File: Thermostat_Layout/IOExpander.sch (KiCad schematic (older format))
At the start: 9 parts, among them J5 Conn_01x04, J6 Conn_01x10, U10 TLP3545, U4 MCP23S17_SO, U8 TLP3545, U9 TLP3545

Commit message: Update schematic
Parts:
- renumbered J5 to J3, J6 to J4, R12 to R10, R10 to R8, R11 to R9, U8 to U5, U4 to U6, U9 to U7, U10 to U8
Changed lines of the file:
@@
 $EndDescr
 $Comp
-L Interface_Expansion:MCP23S17_SO U4
+L Interface_Expansion:MCP23S17_SO U6
 U 1 1 5D3F3897
 P 3750 2800
-F 0 "U4" H 3750 4081 50  0000 C CNN
+F 0 "U6" H 3750 4081 50  0000 C CNN
 F 1 "MCP23S17_SO" H 3750 3990 50  0000 C CNN
 F 2 "Package_SO:SOIC-28W_7.5x17.9mm_P1.27mm" H 3950 1800 50  0001 L CNN
@@
 Connection ~ 3000 3600
 $Comp
-L SparkFun-PowerSymbols:GND #GND0108
+L SparkFun-PowerSymbols:GND #GND012
 U 1 1 5D3F48BE
 P 3750 3900
-F 0 "#GND0108" H 3800 3850 45  0001 L BNN
+F 0 "#GND012" H 3800 3850 45  0001 L BNN
 F 1 "GND" H 3750 3730 45  0000 C CNN
 F 2 "" H 3750 3800 60  0001 C CNN
@@
 Connection ~ 3750 3900
 $Comp
-L SparkFun-PowerSymbols:3.3V #SUPPLY0105
+L SparkFun-PowerSymbols:3.3V #SUPPLY07
 U 1 1 5D3F4F5E
 P 3750 1700
-F 0 "#SUPPLY0105" H 3800 1700 45  0001 L BNN
+F 0 "#SUPPLY07" H 3800 1700 45  0001 L BNN
 F 1 "3.3V" H 3750 1976 45  0000 C CNN
 F 2 "XXX-00000" H 3750 1881 60  0000 C CNN
@@
 	5000 2300 4450 2300
 $Comp
-L Connector_Generic:Conn_01x10 J6
+L Connector_Generic:Conn_01x10 J4
 U 1 1 5D49FB9C
 P 8900 2250
-F 0 "J6" H 8980 2242 50  0000 L CNN
+F 0 "J4" H 8980 2242 50  0000 L CNN
 F 1 "Conn_01x10" H 8980 2151 50  0000 L CNN
 F 2 "Connector_JST:JST_PH_S10B-PH-SM4-TB_1x10-1MP_P2.00mm_Horizontal" H 8900 2250 50  0001 C CNN
@@
 	8700 2550 8000 2550
 $Comp
-L SparkFun-PowerSymbols:GND #GND0118
+L SparkFun-PowerSymbols:GND #GND014
 U 1 1 5D4A3239
 P 8700 2750
-F 0 "#GND0118" H 8750 2700 45  0001 L BNN
+F 0 "#GND014" H 8750 2700 45  0001 L BNN
 F 1 "GND" H 8700 2580 45  0000 C CNN
 F 2 "" H 8700 2650 60  0001 C CNN
@@
 UNUSED_BTN
 $Comp
-L Relay_SolidState:TLP3545 U8
+L Relay_SolidState:TLP3545 U5
 U 1 1 5D4AAA5A
 P 2900 5650
-F 0 "U8" H 2900 5975 50  0000 C CNN
+F 0 "U5" H 2900 5975 50  0000 C CNN
 F 1 "TLP3545" H 2900 5884 50  0000 C CNN
 F 2 "Package_DIP:DIP-6_W7.62mm" H 2900 5350 50  0001 C CNN
@@
 $EndComp
 $Comp
-L Relay_SolidState:TLP3545 U9
+L Relay_SolidState:TLP3545 U7
 U 1 1 5D4B0D89
 P 4000 5650
-F 0 "U9" H 4000 5975 50  0000 C CNN
+F 0 "U7" H 4000 5975 50  0000 C CNN
 F 1 "TLP3545" H 4000 5884 50  0000 C CNN
 F 2 "Package_DIP:DIP-6_W7.62mm" H 4000 5350 50  0001 C CNN
@@
 $EndComp
 $Comp
-L Relay_SolidState:TLP3545 U10
+L Relay_SolidState:TLP3545 U8
 U 1 1 5D4B27F7
 P 5100 5650
-F 0 "U10" H 5100 5975 50  0000 C CNN
+F 0 "U8" H 5100 5975 50  0000 C CNN
 F 1 "TLP3545" H 5100 5884 50  0000 C CNN
 F 2 "Package_DIP:DIP-6_W7.62mm" H 5100 5350 50  0001 C CNN
@@
 $EndComp
 $Comp
-L Device:R_US R10
+L Device:R_US R8
 U 1 1 5D4B3F71
 P 2450 5900
-F 0 "R10" H 2518 5946 50  0000 L CNN
+F 0 "R8" H 2518 5946 50  0000 L CNN
 F 1 "100Ω" H 2518 5855 50  0000 L CNN
 F 2 "Resistor_SMD:R_0402_1005Metric" V 2490 5890 50  0001 C CNN
@@
 $EndComp
 $Comp
-L Device:R_US R11
+L Device:R_US R9
 U 1 1 5D4B4905
 P 3550 5900
-F 0 "R11" H 3618 5946 50  0000 L CNN
+F 0 "R9" H 3618 5946 50  0000 L CNN
 F 1 "100Ω" H 3618 5855 50  0000 L CNN
 F 2 "Resistor_SMD:R_0402_1005Metric" V 3590 5890 50  0001 C CNN
@@
 $EndComp
 $Comp
-L Device:R_US R12
+L Device:R_US R10
 U 1 1 5D4B5111
 P 4650 5900
-F 0 "R12" H 4718 5946 50  0000 L CNN
+F 0 "R10" H 4718 5946 50  0000 L CNN
 F 1 "100Ω" H 4718 5855 50  0000 L CNN
 F 2 "Resistor_SMD:R_0402_1005Metric" V 4690 5890 50  0001 C CNN
@@
 	4650 5750 4800 5750
 $Comp
-L SparkFun-PowerSymbols:GND #GND0119
+L SparkFun-PowerSymbols:GND #GND010
 U 1 1 5D4B7A1D
 P 2450 6050
-F 0 "#GND0119" H 2500 6000 45  0001 L BNN
+F 0 "#GND010" H 2500 6000 45  0001 L BNN
 F 1 "GND" H 2450 5880 45  0000 C CNN
 F 2 "" H 2450 5950 60  0001 C CNN
@@
 $EndComp
 $Comp
-L SparkFun-PowerSymbols:GND #GND0120
+L SparkFun-PowerSymbols:GND #GND011
 U 1 1 5D4C6759
 P 3550 6050
-F 0 "#GND0120" H 3600 6000 45  0001 L BNN
+F 0 "#GND011" H 3600 6000 45  0001 L BNN
 F 1 "GND" H 3550 5880 45  0000 C CNN
 F 2 "" H 3550 5950 60  0001 C CNN
@@
 $EndComp
 $Comp
-L SparkFun-PowerSymbols:GND #GND0121
+L SparkFun-PowerSymbols:GND #GND013
 U 1 1 5D4C6D83
 P 4650 6050
-F 0 "#GND0121" H 4700 6000 45  0001 L BNN
+F 0 "#GND013" H 4700 6000 45  0001 L BNN
 F 1 "GND" H 4650 5880 45  0000 C CNN
 F 2 "" H 4650 5950 60  0001 C CNN
@@
 FAN_ON
 $Comp
-L Connector_Generic:Conn_01x04 J5
+L Connector_Generic:Conn_01x04 J3
 U 1 1 5D4F7015
 P 8850 4050
-F 0 "J5" H 8930 4042 50  0000 L CNN
+F 0 "J3" H 8930 4042 50  0000 L CNN
 F 1 "Conn_01x04" H 8930 3951 50  0000 L CNN
 F 2 "TerminalBlock_TE-Connectivity:TerminalBlock_TE_282834-4_1x04_P2.54mm_Horizontal" H 8850 4050 50  0001 C CNN

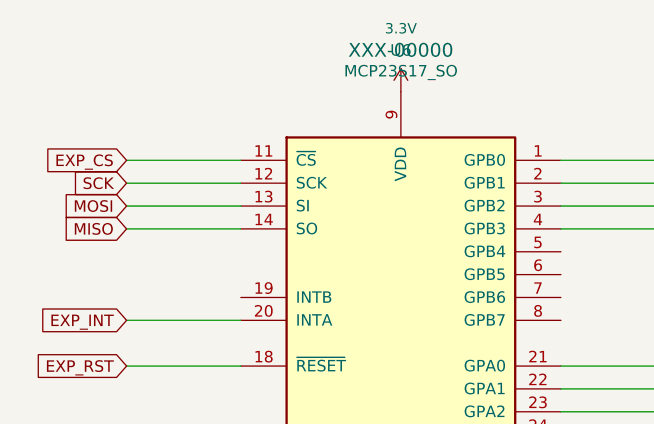
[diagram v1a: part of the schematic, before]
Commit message: Swap out the MCP23s17 for the MCP23017
Removes the need for the SPI bus
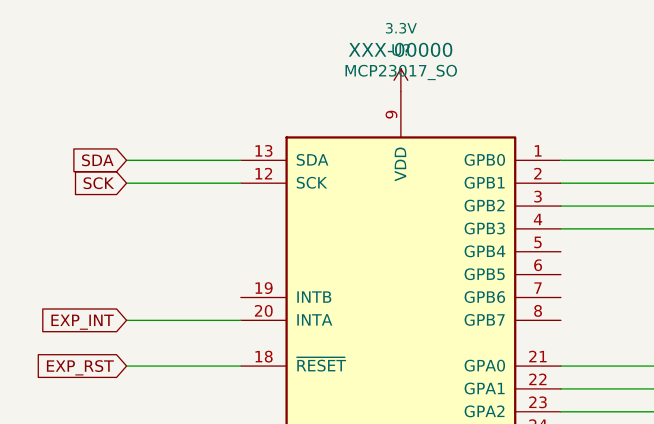
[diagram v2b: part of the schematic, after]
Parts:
- removed U6: MCP23S17_SO, Package_SO:SOIC-28W_7.5x17.9mm_P1.27mm, symbol Interface_Expansion:MCP23S17_SO
- added U?: MCP23017_SO, Package_SO:SOIC-28W_7.5x17.9mm_P1.27mm, symbol Interface_Expansion:MCP23017_SO
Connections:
- net 3.3V: now also U?.9 (VDD)
- net COOL_ON: now also U?.2 (GPB1)
- net DWN_BTN: now also U?.22 (GPA1)
- net EXP_INT: now also U?.20 (INTA)
- net EXP_RST: now also U?.18 (~RESET~)
- net FAN_BTN: now also U?.24 (GPA3)
- net FAN_ON: now also U?.3 (GPB2)
- net GND: now also U?.10 (VSS), U?.15 (A0), U?.16 (A1), U?.17 (A2)
- net HEAT_ON: now also U?.1 (GPB0)
- net LCD_LED: now also U?.4 (GPB3)
- net MODE_BTN: now also U?.23 (GPA2)
- net REMOTE_BTN: now also U?.26 (GPA5)
- net SCHED_BTN: now also U?.27 (GPA6)
- net SCK: now also U?.12 (SCK)
- net SETTINGS_BTN: now also U?.25 (GPA4)
- net UNUSED_BTN: now also U?.28 (GPA7)
- net UP_BTN: now also U?.21 (GPA0)
- new net SDA: U?.13 (SDA)
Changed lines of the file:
@@
 Comment4 ""
 $EndDescr
-$Comp
-L Interface_Expansion:MCP23S17_SO U6
-U 1 1 5D3F3897
-P 3750 2800
-F 0 "U6" H 3750 4081 50  0000 C CNN
-F 1 "MCP23S17_SO" H 3750 3990 50  0000 C CNN
-F 2 "Package_SO:SOIC-28W_7.5x17.9mm_P1.27mm" H 3950 1800 50  0001 L CNN
-F 3 "http://ww1.microchip.com/downloads/en/DeviceDoc/20001952C.pdf" H 3950 1700 50  0001 L CNN
-	1    3750 2800
-	1    0    0    -1
-$EndComp
 Wire Wire Line
 	3050 3400 3000 3400
@@
 	1    0    0    -1
 $EndComp
-Connection ~ 3750 3900
 $Comp
 L SparkFun-PowerSymbols:3.3V #SUPPLY07
@@
 Wire Wire Line
 	3050 2100 2550 2100
-Wire Wire Line
-	3050 2200 2550 2200
-Wire Wire Line
-	3050 2300 2550 2300
 Text GLabel 2550 2700 0    50   Input ~ 0
 EXP_INT
 Text GLabel 2550 2900 0    50   Input ~ 0
 EXP_RST
-Text GLabel 2550 2300 0    50   Input ~ 0
-MISO
-Text GLabel 2550 2200 0    50   Input ~ 0
-MOSI
 Text GLabel 2550 2100 0    50   Input ~ 0
 SCK
 Text GLabel 2550 2000 0    50   Input ~ 0
-EXP_CS
+SDA
 Wire Wire Line
 	4450 2900 5000 2900
@@
 Text GLabel 8100 4250 0    50   Input ~ 0
 COMMON
+$Comp
+L Interface_Expansion:MCP23017_SO U?
+U 1 1 5DA26DAE
+P 3750 2800
+F 0 "U?" H 3750 4081 50  0000 C CNN
+F 1 "MCP23017_SO" H 3750 3990 50  0000 C CNN
+F 2 "Package_SO:SOIC-28W_7.5x17.9mm_P1.27mm" H 3950 1800 50  0001 L CNN
+F 3 "http://ww1.microchip.com/downloads/en/DeviceDoc/20001952C.pdf" H 3950 1700 50  0001 L CNN
+	1    3750 2800
+	1    0    0    -1
+$EndComp
+Connection ~ 3750 3900
 $EndSCHEMATC

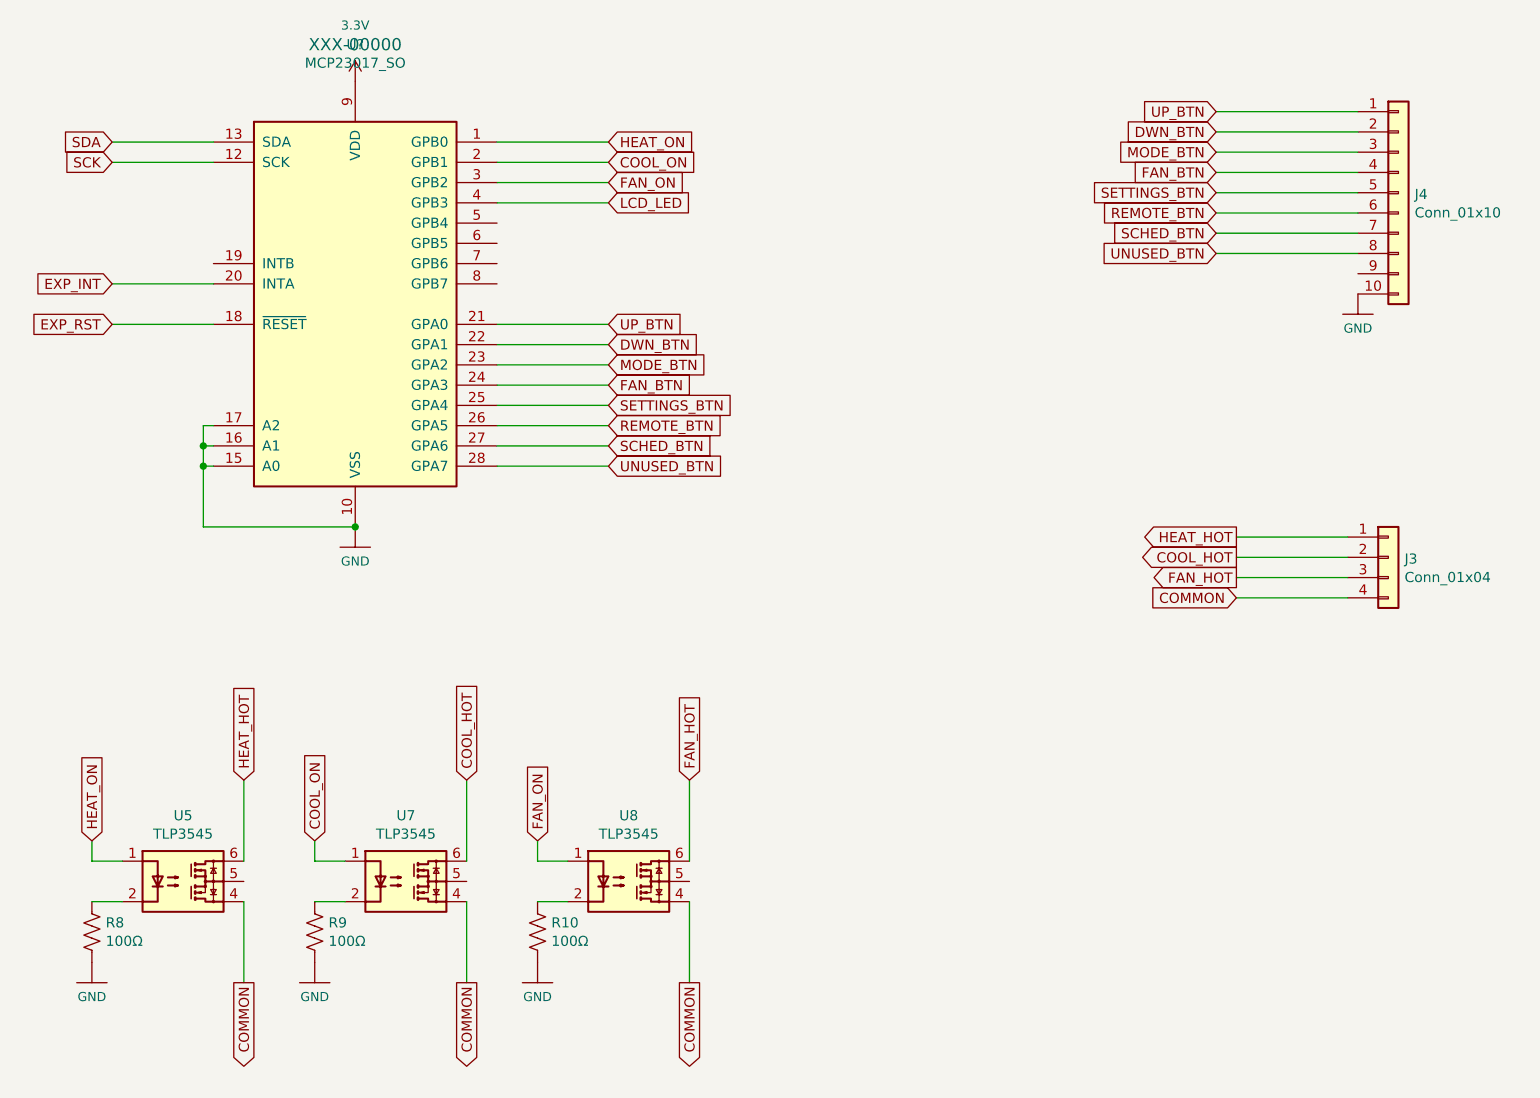
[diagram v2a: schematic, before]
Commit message: FInalize schematic for thermostat
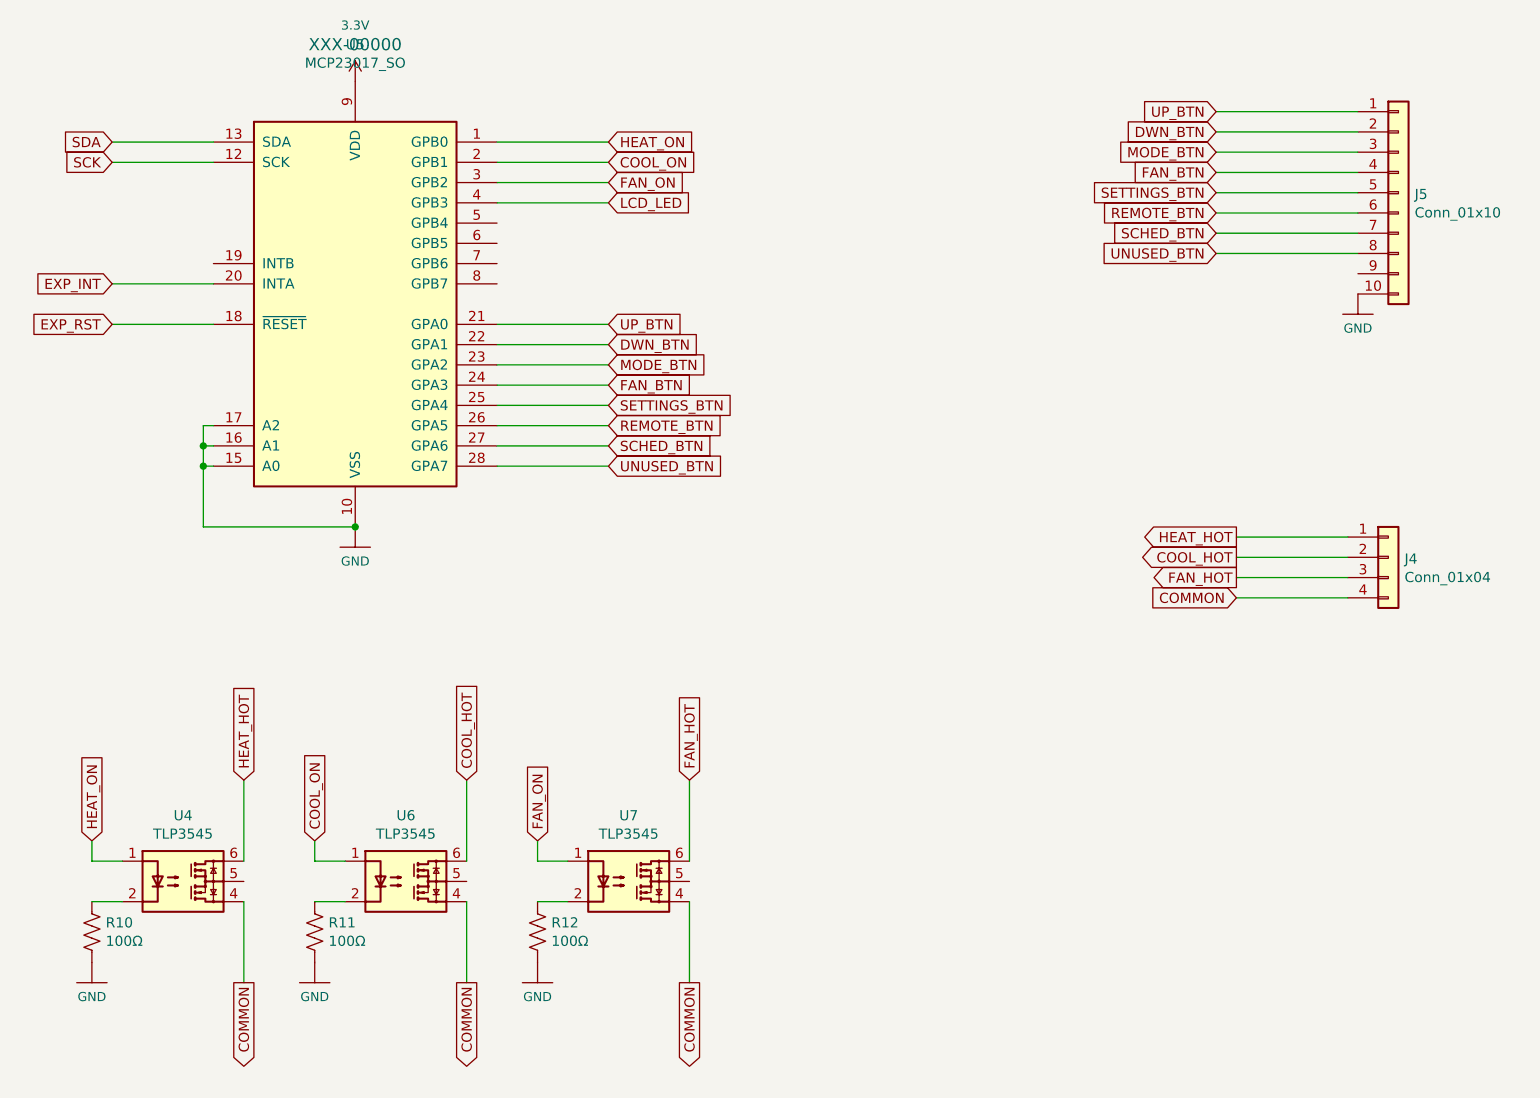
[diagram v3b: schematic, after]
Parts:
- gave numbers to parts that had none: 1
- renumbered J3 to J4, J4 to J5, R8 to R10, R9 to R11, R10 to R12, U5 to U4, U7 to U6, U8 to U7
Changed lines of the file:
@@
 Connection ~ 3000 3600
 $Comp
-L SparkFun-PowerSymbols:GND #GND012
+L SparkFun-PowerSymbols:GND #GND010
 U 1 1 5D3F48BE
 P 3750 3900
-F 0 "#GND012" H 3800 3850 45  0001 L BNN
+F 0 "#GND010" H 3800 3850 45  0001 L BNN
 F 1 "GND" H 3750 3730 45  0000 C CNN
 F 2 "" H 3750 3800 60  0001 C CNN
@@
 $EndComp
 $Comp
-L SparkFun-PowerSymbols:3.3V #SUPPLY07
+L SparkFun-PowerSymbols:3.3V #SUPPLY06
 U 1 1 5D3F4F5E
 P 3750 1700
-F 0 "#SUPPLY07" H 3800 1700 45  0001 L BNN
+F 0 "#SUPPLY06" H 3800 1700 45  0001 L BNN
 F 1 "3.3V" H 3750 1976 45  0000 C CNN
 F 2 "XXX-00000" H 3750 1881 60  0000 C CNN
@@
 	5000 2300 4450 2300
 $Comp
-L Connector_Generic:Conn_01x10 J4
+L Connector_Generic:Conn_01x10 J5
 U 1 1 5D49FB9C
 P 8900 2250
-F 0 "J4" H 8980 2242 50  0000 L CNN
+F 0 "J5" H 8980 2242 50  0000 L CNN
 F 1 "Conn_01x10" H 8980 2151 50  0000 L CNN
 F 2 "Connector_JST:JST_PH_S10B-PH-SM4-TB_1x10-1MP_P2.00mm_Horizontal" H 8900 2250 50  0001 C CNN
@@
 	8700 2550 8000 2550
 $Comp
-L SparkFun-PowerSymbols:GND #GND014
+L SparkFun-PowerSymbols:GND #GND012
 U 1 1 5D4A3239
 P 8700 2750
-F 0 "#GND014" H 8750 2700 45  0001 L BNN
+F 0 "#GND012" H 8750 2700 45  0001 L BNN
 F 1 "GND" H 8700 2580 45  0000 C CNN
 F 2 "" H 8700 2650 60  0001 C CNN
@@
 UNUSED_BTN
 $Comp
-L Relay_SolidState:TLP3545 U5
+L Relay_SolidState:TLP3545 U4
 U 1 1 5D4AAA5A
 P 2900 5650
-F 0 "U5" H 2900 5975 50  0000 C CNN
+F 0 "U4" H 2900 5975 50  0000 C CNN
 F 1 "TLP3545" H 2900 5884 50  0000 C CNN
 F 2 "Package_DIP:DIP-6_W7.62mm" H 2900 5350 50  0001 C CNN
@@
 $EndComp
 $Comp
-L Relay_SolidState:TLP3545 U7
+L Relay_SolidState:TLP3545 U6
 U 1 1 5D4B0D89
 P 4000 5650
-F 0 "U7" H 4000 5975 50  0000 C CNN
+F 0 "U6" H 4000 5975 50  0000 C CNN
 F 1 "TLP3545" H 4000 5884 50  0000 C CNN
 F 2 "Package_DIP:DIP-6_W7.62mm" H 4000 5350 50  0001 C CNN
@@
 $EndComp
 $Comp
-L Relay_SolidState:TLP3545 U8
+L Relay_SolidState:TLP3545 U7
 U 1 1 5D4B27F7
 P 5100 5650
-F 0 "U8" H 5100 5975 50  0000 C CNN
+F 0 "U7" H 5100 5975 50  0000 C CNN
 F 1 "TLP3545" H 5100 5884 50  0000 C CNN
 F 2 "Package_DIP:DIP-6_W7.62mm" H 5100 5350 50  0001 C CNN
@@
 $EndComp
 $Comp
-L Device:R_US R8
+L Device:R_US R10
 U 1 1 5D4B3F71
 P 2450 5900
-F 0 "R8" H 2518 5946 50  0000 L CNN
+F 0 "R10" H 2518 5946 50  0000 L CNN
 F 1 "100Ω" H 2518 5855 50  0000 L CNN
 F 2 "Resistor_SMD:R_0402_1005Metric" V 2490 5890 50  0001 C CNN
@@
 $EndComp
 $Comp
-L Device:R_US R9
+L Device:R_US R11
 U 1 1 5D4B4905
 P 3550 5900
-F 0 "R9" H 3618 5946 50  0000 L CNN
+F 0 "R11" H 3618 5946 50  0000 L CNN
 F 1 "100Ω" H 3618 5855 50  0000 L CNN
 F 2 "Resistor_SMD:R_0402_1005Metric" V 3590 5890 50  0001 C CNN
@@
 $EndComp
 $Comp
-L Device:R_US R10
+L Device:R_US R12
 U 1 1 5D4B5111
 P 4650 5900
-F 0 "R10" H 4718 5946 50  0000 L CNN
+F 0 "R12" H 4718 5946 50  0000 L CNN
 F 1 "100Ω" H 4718 5855 50  0000 L CNN
 F 2 "Resistor_SMD:R_0402_1005Metric" V 4690 5890 50  0001 C CNN
@@
 	4650 5750 4800 5750
 $Comp
-L SparkFun-PowerSymbols:GND #GND010
+L SparkFun-PowerSymbols:GND #GND08
 U 1 1 5D4B7A1D
 P 2450 6050
-F 0 "#GND010" H 2500 6000 45  0001 L BNN
+F 0 "#GND08" H 2500 6000 45  0001 L BNN
 F 1 "GND" H 2450 5880 45  0000 C CNN
 F 2 "" H 2450 5950 60  0001 C CNN
@@
 $EndComp
 $Comp
-L SparkFun-PowerSymbols:GND #GND011
+L SparkFun-PowerSymbols:GND #GND09
 U 1 1 5D4C6759
 P 3550 6050
-F 0 "#GND011" H 3600 6000 45  0001 L BNN
+F 0 "#GND09" H 3600 6000 45  0001 L BNN
 F 1 "GND" H 3550 5880 45  0000 C CNN
 F 2 "" H 3550 5950 60  0001 C CNN
@@
 $EndComp
 $Comp
-L SparkFun-PowerSymbols:GND #GND013
+L SparkFun-PowerSymbols:GND #GND011
 U 1 1 5D4C6D83
 P 4650 6050
-F 0 "#GND013" H 4700 6000 45  0001 L BNN
+F 0 "#GND011" H 4700 6000 45  0001 L BNN
 F 1 "GND" H 4650 5880 45  0000 C CNN
 F 2 "" H 4650 5950 60  0001 C CNN
@@
 FAN_ON
 $Comp
-L Connector_Generic:Conn_01x04 J3
+L Connector_Generic:Conn_01x04 J4
 U 1 1 5D4F7015
 P 8850 4050
-F 0 "J3" H 8930 4042 50  0000 L CNN
+F 0 "J4" H 8930 4042 50  0000 L CNN
 F 1 "Conn_01x04" H 8930 3951 50  0000 L CNN
 F 2 "TerminalBlock_TE-Connectivity:TerminalBlock_TE_282834-4_1x04_P2.54mm_Horizontal" H 8850 4050 50  0001 C CNN
@@
 COMMON
 $Comp
-L Interface_Expansion:MCP23017_SO U?
+L Interface_Expansion:MCP23017_SO U5
 U 1 1 5DA26DAE
 P 3750 2800
-F 0 "U?" H 3750 4081 50  0000 C CNN
+F 0 "U5" H 3750 4081 50  0000 C CNN
 F 1 "MCP23017_SO" H 3750 3990 50  0000 C CNN
 F 2 "Package_SO:SOIC-28W_7.5x17.9mm_P1.27mm" H 3950 1800 50  0001 L CNN
